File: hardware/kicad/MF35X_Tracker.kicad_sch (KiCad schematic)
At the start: 15 parts, among them J1 To external solenoid-valve dr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, J2 5 V DC/DC input, J3 VDO 801/1/6 oil-temperature s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, J4 Oil-pressure sender, J5 Vehicle battery sense + / GND, J6 K-type thermocouple T+ / T-, U1 Freenove ESP32-S3 WROOM Lite 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, U2 ADS1115 @ 0x48, U3 ATGM336H GPS / UART 115200 / 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, U4 MAX31855 K-type, U5 HY-M154 optocoupler / RPM W-t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

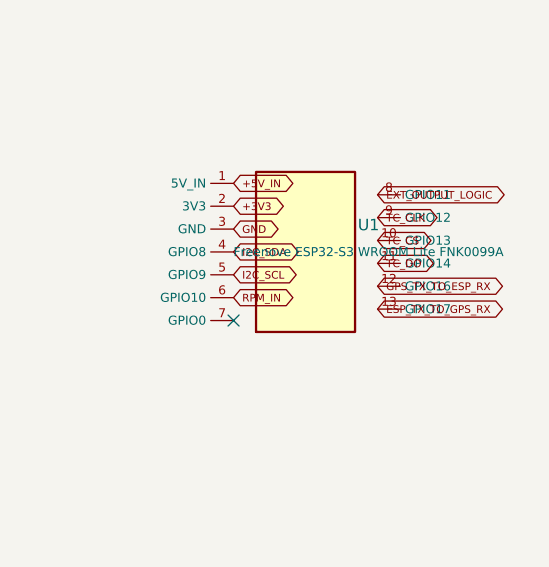
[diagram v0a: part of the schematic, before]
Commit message: Regenerate KiCad with external power flags
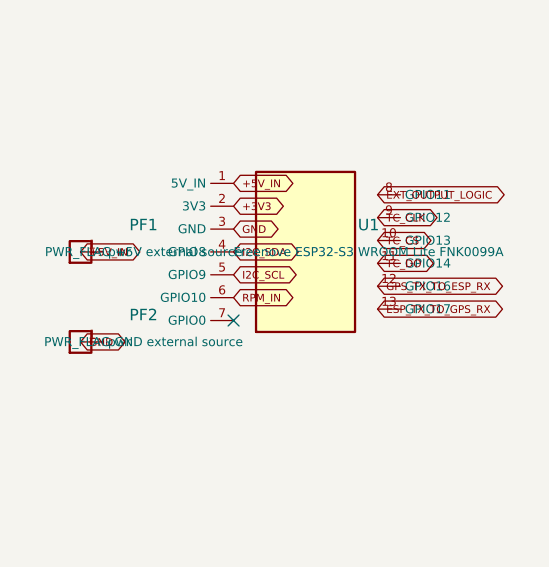
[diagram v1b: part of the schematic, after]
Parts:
- added PF1: PWR_FLAG +5V external source, symbol power:PWR_FLAG
- added PF2: PWR_FLAG GND external source, symbol power:PWR_FLAG
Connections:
- net +5V_IN: now also PF1.1 (pwr)
- net GND: now also PF2.1 (pwr)
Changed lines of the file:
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@@
     (instances (project "MF35X_Tracker" (path "/7c44dcb5-b2e5-41b8-9fe6-5d37a9a1d001" (reference "J6") (unit 1))))
+  )
+  (symbol (lib_id "power:PWR_FLAG") (at 25.00 55.00 0) (unit 1)
+    (in_bom no) (on_board no)
+    (property "Reference" "PF1" (at 32.00 52.00 0) (effects (font (size 1.27 1.27))))
+    (property "Value" "PWR_FLAG +5V external source" (at 32.00 55.00 0) (effects (font (size 1.0 1.0))))
+    (property "Footprint" "" (at 25.00 55.00 0) (effects (font (size 1.27 1.27)) hide))
+    (property "Datasheet" "~" (at 25.00 55.00 0) (effects (font (size 1.27 1.27)) hide))
+    (pin "1")
+    (instances (project "MF35X_Tracker" (path "/7c44dcb5-b2e5-41b8-9fe6-5d37a9a1d001" (reference "PF1") (unit 1))))
+  )
+  (symbol (lib_id "power:PWR_FLAG") (at 25.00 65.00 0) (unit 1)
+    (in_bom no) (on_board no)
+    (property "Reference" "PF2" (at 32.00 62.00 0) (effects (font (size 1.27 1.27))))
+    (property "Value" "PWR_FLAG GND external source" (at 32.00 65.00 0) (effects (font (size 1.0 1.0))))
+    (property "Footprint" "" (at 25.00 65.00 0) (effects (font (size 1.27 1.27)) hide))
+    (property "Datasheet" "~" (at 25.00 65.00 0) (effects (font (size 1.27 1.27)) hide))
+    (pin "1")
+    (instances (project "MF35X_Tracker" (path "/7c44dcb5-b2e5-41b8-9fe6-5d37a9a1d001" (reference "PF2") (unit 1))))
   )
   (global_label "EXT_OUTPUT_LOGIC" (shape bidirectional) (at 42.00 98.73 0)
@@
     (effects (font (size 0.85 0.85)) (justify left))
   )
+  (global_label "+5V_IN" (shape bidirectional) (at 25.00 55.00 0)
+    (effects (font (size 0.85 0.85)) (justify left))
+  )
+  (global_label "GND" (shape bidirectional) (at 25.00 65.00 0)
+    (effects (font (size 0.85 0.85)) (justify left))
+  )
